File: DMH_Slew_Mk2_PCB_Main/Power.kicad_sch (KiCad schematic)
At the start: 13 parts, among them J0 Conn_01x01, J100 IDC_02x08, J200 IDC_02x05, U10 LM4040LP-10

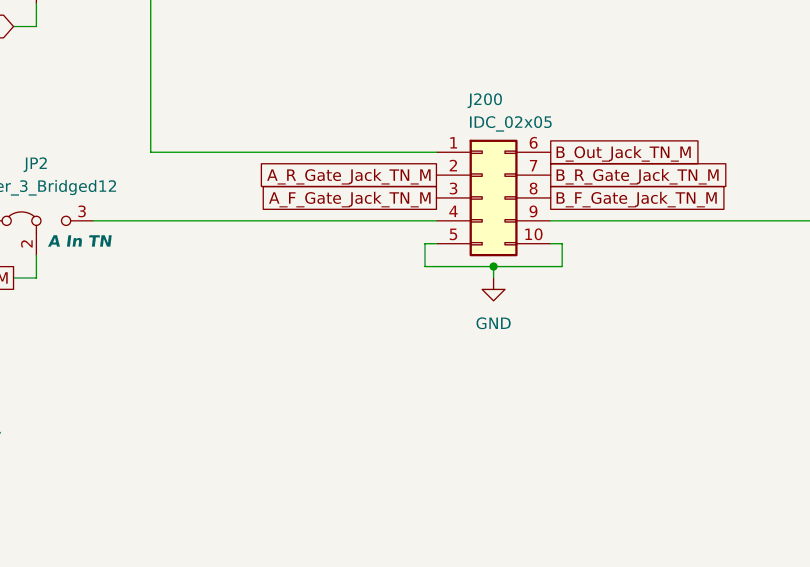
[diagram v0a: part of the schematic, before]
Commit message: Redesigned panel and main PCB schematic
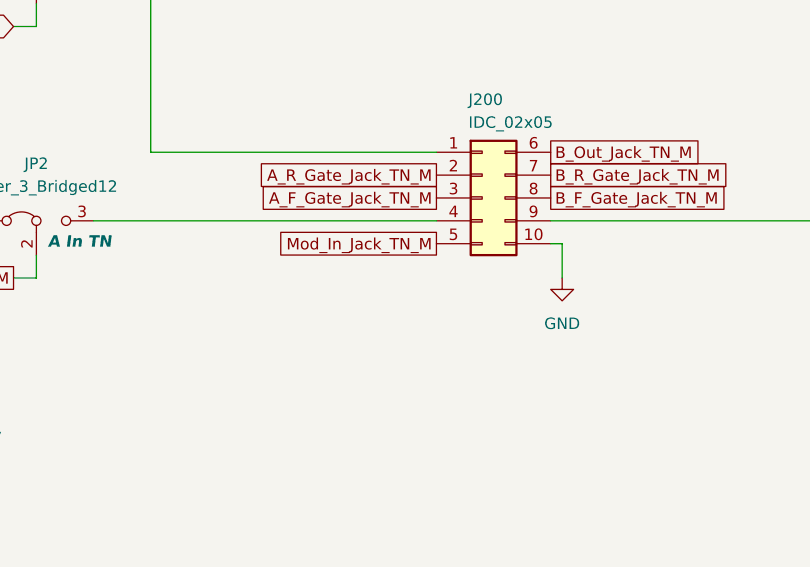
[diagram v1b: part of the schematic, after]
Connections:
- net GND: no longer J200.5 (Pin_5)
- new net Mod_In_Jack_TN_M: J200.5 (Pin_5)
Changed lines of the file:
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@@
-		(color 0 0 0 0)
-	)
-	(junction
-		(at 165.1 134.62)
-		(diameter 0)
 		(color 0 0 0 0)
 	)
@@
 	(wire
 		(pts
-			(xy 157.48 134.62) (xy 165.1 134.62)
-		)
-		(stroke
-			(width 0)
-			(type default)
-		)
-	)
-	(wire
-		(pts
 			(xy 34.29 165.1) (xy 34.29 185.42)
 		)
@@
 	(wire
 		(pts
-			(xy 172.72 134.62) (xy 165.1 134.62)
-		)
-		(stroke
-			(width 0)
-			(type default)
-		)
-	)
-	(wire
-		(pts
 			(xy 218.44 135.89) (xy 215.9 135.89)
 		)
@@
 	(wire
 		(pts
-			(xy 157.48 132.08) (xy 157.48 134.62)
-		)
-		(stroke
-			(width 0)
-			(type default)
-		)
-	)
-	(wire
-		(pts
 			(xy 19.05 182.88) (xy 13.97 182.88)
 		)
@@
 	(wire
 		(pts
-			(xy 172.72 132.08) (xy 172.72 134.62)
-		)
-		(stroke
-			(width 0)
-			(type default)
-		)
-	)
-	(wire
-		(pts
 			(xy 63.5 95.25) (xy 63.5 104.14)
 		)
@@
 	(wire
 		(pts
-			(xy 165.1 134.62) (xy 165.1 135.89)
+			(xy 172.72 132.08) (xy 172.72 135.89)
 		)
 		(stroke
@@
 		(pts
 			(xy 101.6 129.54) (xy 107.95 129.54)
-		)
-		(stroke
-			(width 0)
-			(type default)
-		)
-	)
-	(wire
-		(pts
-			(xy 158.75 132.08) (xy 157.48 132.08)
 		)
 		(stroke
@@
 				)
 				(justify left)
+				(hide yes)
+			)
+		)
+	)
+	(global_label "Mod_In_Jack_TN_M"
+		(shape passive)
+		(at 158.75 132.08 180)
+		(fields_autoplaced yes)
+		(effects
+			(font
+				(size 1.27 1.27)
+			)
+			(justify right)
+		)
+		(property "Intersheetrefs" "${INTERSHEET_REFS}"
+			(at 139.5197 132.08 0)
+			(effects
+				(font
+					(size 1.27 1.27)
+				)
+				(justify right)
 				(hide yes)
 			)
@@
 	(symbol
 		(lib_id "power:GND")
-		(at 165.1 135.89 0)
+		(at 172.72 135.89 0)
 		(unit 1)
 		(exclude_from_sim no)
@@
 		(fields_autoplaced yes)
 		(property "Reference" "#PWR047"
-			(at 165.1 142.24 0)
+			(at 172.72 142.24 0)
 			(effects
 				(font
@@
 		)
 		(property "Value" "GND"
-			(at 165.1 140.97 0)
+			(at 172.72 140.97 0)
 			(effects
 				(font
@@
 		)
 		(property "Footprint" ""
-			(at 165.1 135.89 0)
+			(at 172.72 135.89 0)
 			(effects
 				(font
@@
 		)
 		(property "Datasheet" ""
-			(at 165.1 135.89 0)
+			(at 172.72 135.89 0)
 			(effects
 				(font
@@
 		)
 		(property "Description" "Power symbol creates a global label with name \"GND\" , ground"
-			(at 165.1 135.89 0)
-			(effects
-				(font
+			(at 172.72 135.89 0)
+			(effects
+				(font
